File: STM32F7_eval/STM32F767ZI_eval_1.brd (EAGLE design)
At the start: 76.2 x 53.3 mm, 89 parts, among them CN1 GROVE-4P-CONN-I2C-90D, CN2 GROVE-4P-CONN-I2C-90D, CN3 GROVE-4P-CONN-I2C-90D, CN4 GROVE-4P-CONN-AN01-90D, CN5 ARDUINO_COMPAT_IF, CN6 STLINKV21_SWD_IF, CN7 WFT0750CZ09-SMD_, CN8 MCO_IF, CN9 UART_IF, Q1 PMF370XN_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

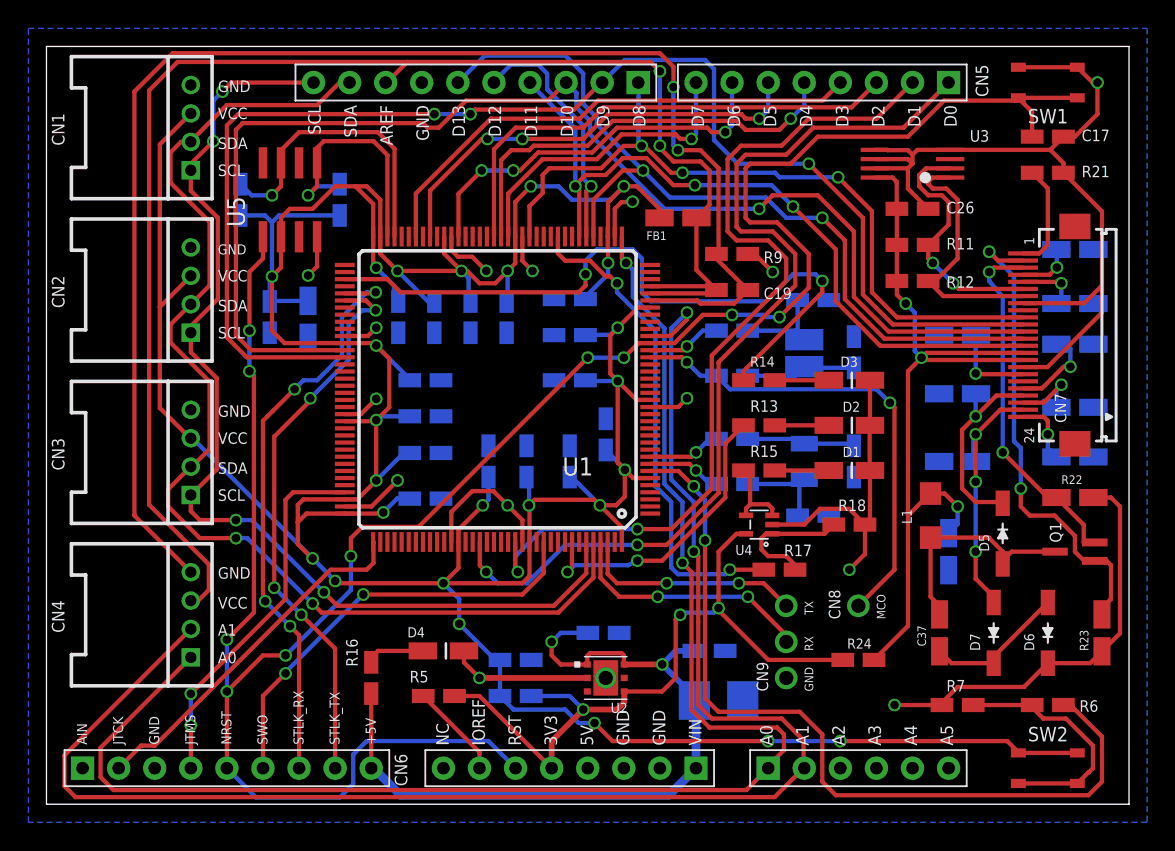
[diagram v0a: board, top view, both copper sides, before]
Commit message: 評価基板を修正
・手はんだ用パターンに修正
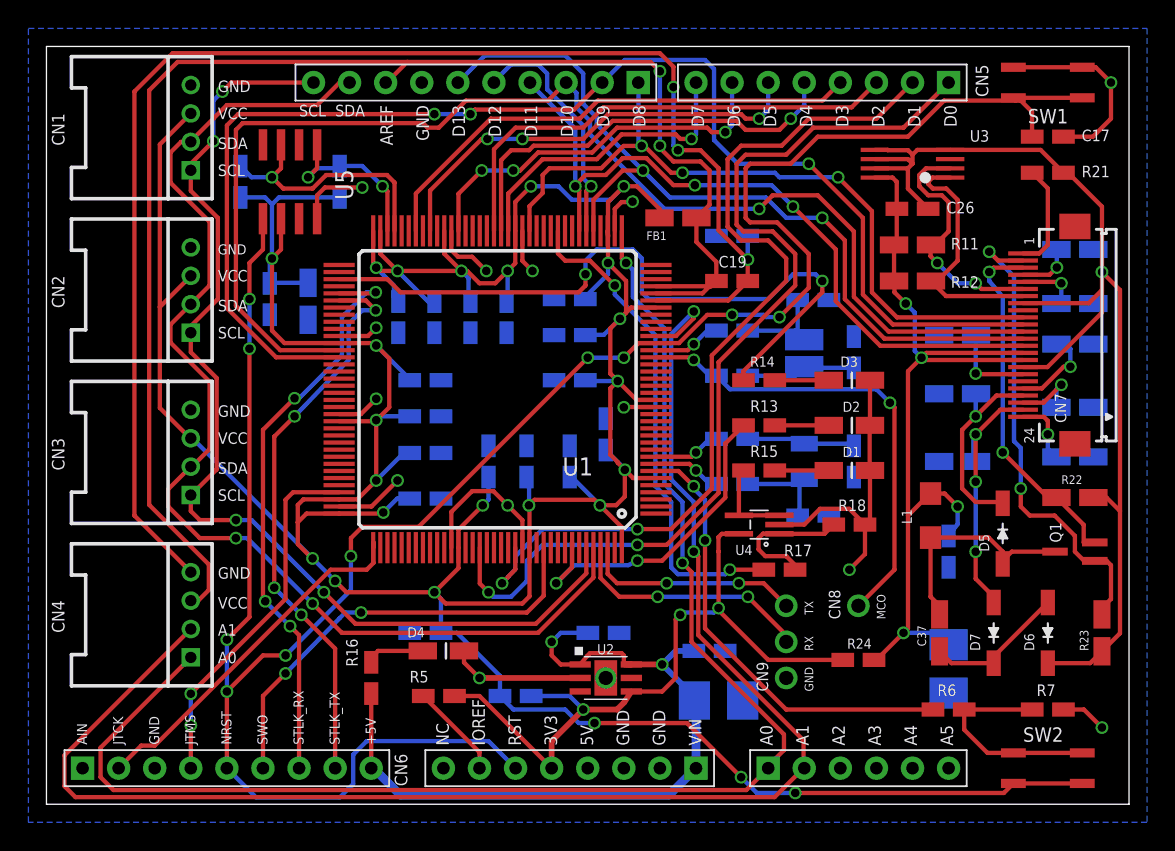
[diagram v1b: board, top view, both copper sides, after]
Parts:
- added C39: 10uF, Parts:C1210_TPST_DEV
- C38: device Parts:SMD_2012_DEV -> Parts:SMD_1608_DEV
- R11, R12: device Parts:SMD_1608_DEV -> Parts:SMD_2012_DEV
- SW1, SW2: value SKRPACE010 -> SKRPACE010_; device Parts:SKRPACE010 -> Parts:SKRPACE010_DEV
- U1: value STM32F767ZI -> STM32F767ZI_; device Parts:LQFP144 -> Parts:LQFP144_DEV
- U2: value LD39050PU33R -> LD39050PU33R_DEV; device Parts:DFN6-3X3 -> Parts:DFN6-3X3_
- U4: value TSV631AICT -> TSV631AICT_; device Parts:SC-70-5 -> Parts:SC-70-5_DEV
- moved R6 6.99 mm to (63.5, 6.67), turned to 0 degrees
- moved C22 6.63 mm to (26.7, 12.1), turned to 0 degrees
- moved R7 6.36 mm to (70.5, 6.67), turned to 180 degrees
- moved C28 1.27 mm to (15.7, 35.6)
- moved R9 1.27 mm to (48.3, 40.0), flipped to the bottom
- moved C29 1.27 mm to (18.4, 35.4)
- moved R19 1.27 mm to (13.7, 43.8)
- moved R20 1.27 mm to (20.6, 43.8)
- moved U5 1.27 mm to (17.1, 43.8)
- moved C19 0.63 mm to (48.3, 36.8)
- turned SW2 to 0 degrees
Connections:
- net 0V: now also C39.2
- net VCC_EPD: now also C39.1
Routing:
- net PC13: track 58.7 -> 31.8 mm
- net 0V: track 160.5 -> 170.2 mm
- net PB11: track 17.4 -> 12.0 mm, vias 1 -> 2
- net VCC_EPD: track 58.6 -> 62.5 mm, vias 3 -> 4
- net PB10: track 21.2 -> 18.1 mm
- net PB7: track 21.1 -> 23.7 mm
- net PC0: track 110.8 -> 108.3 mm
- net PA3: track 104.5 -> 102.1 mm
- net N$6: track 17.5 -> 15.2 mm
- net PG9: track 67.3 -> 69.2 mm
- net AVDD: track 106.1 -> 104.3 mm
- net NRST: track 158.5 -> 160.2 mm
- net PD15: track 95.6 -> 93.9 mm
- net PD14: track 91.5 -> 89.9 mm
- net PG14: track 62.8 -> 64.4 mm
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
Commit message: 評価基板を修正
・シルクの位置などを調整
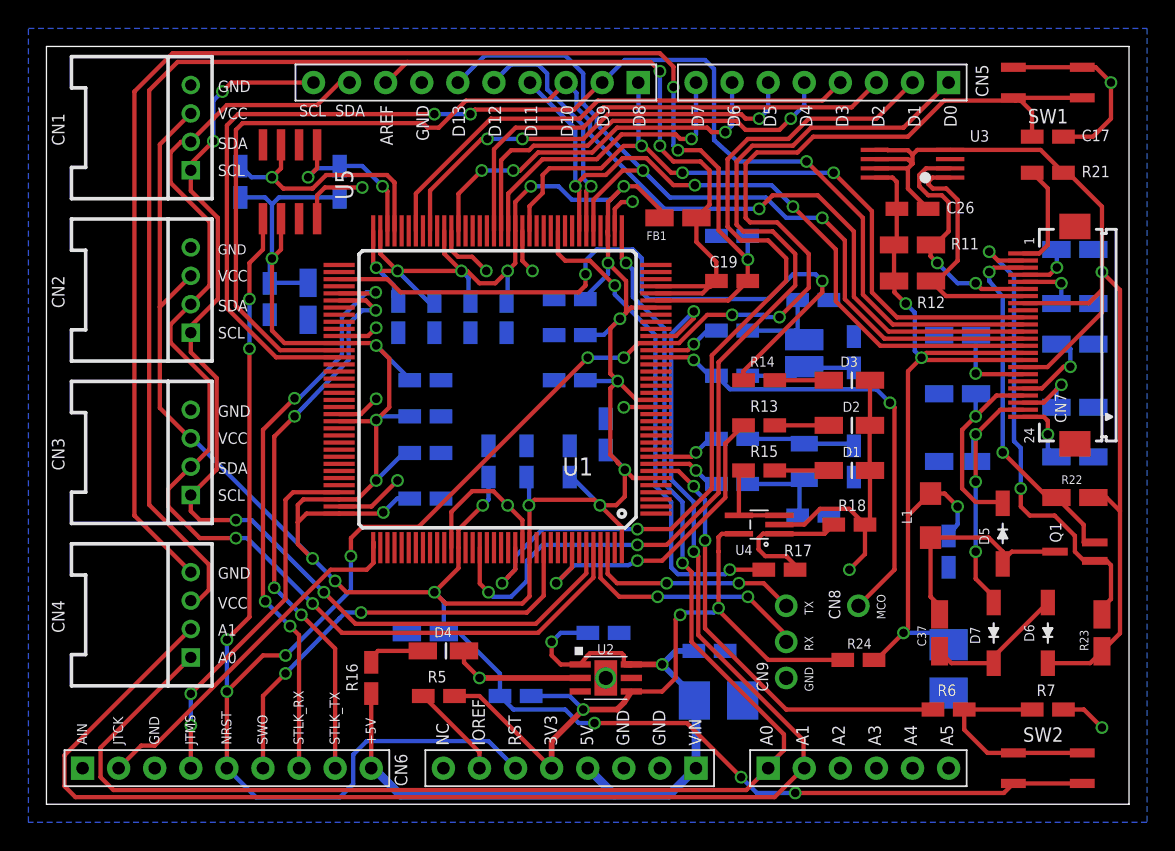
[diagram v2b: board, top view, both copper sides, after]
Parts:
- C22: device Parts:SMD_1608_DEV -> Parts:SMD_2012_DEV
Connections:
- net VIN: now also CN5.23
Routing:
- net VIN: track 55.5 -> 58.2 mm

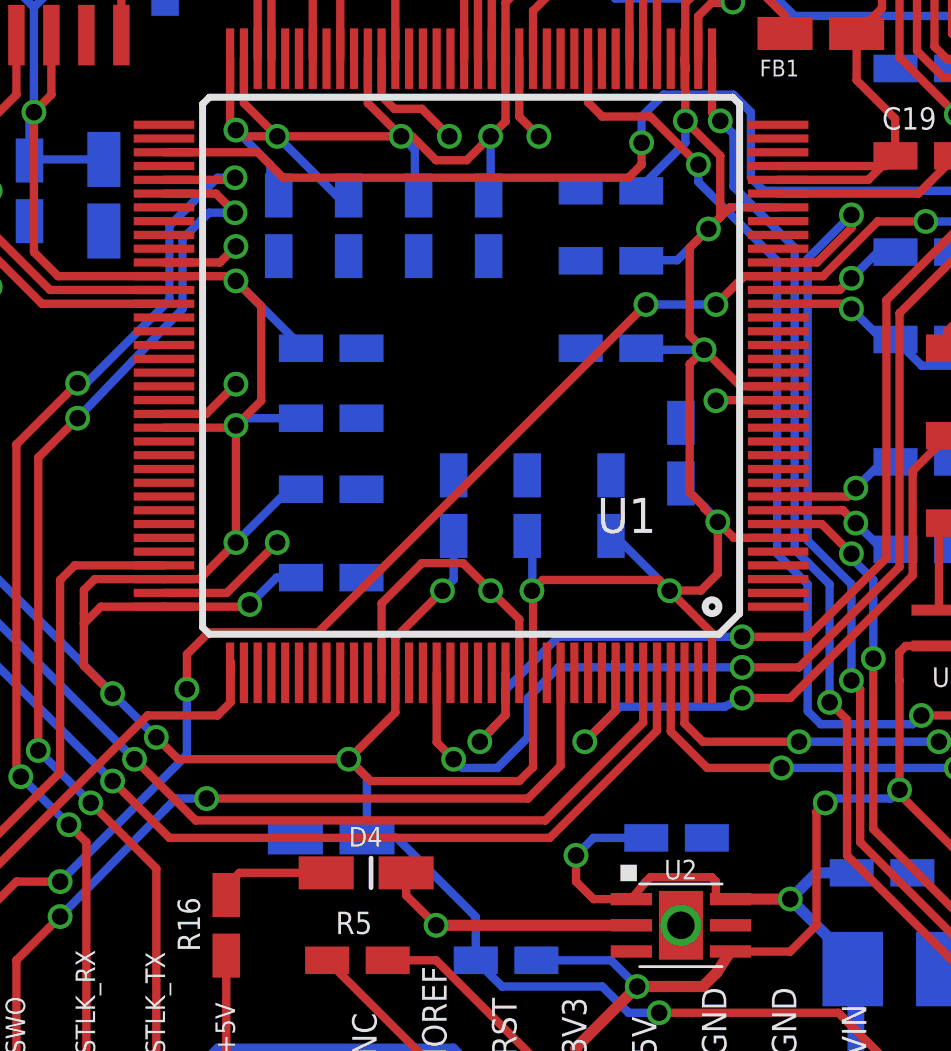
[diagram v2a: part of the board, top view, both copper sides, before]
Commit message: 評価基板を修正
・バイパスコンデンサー修正
・配線欠落箇所を修正
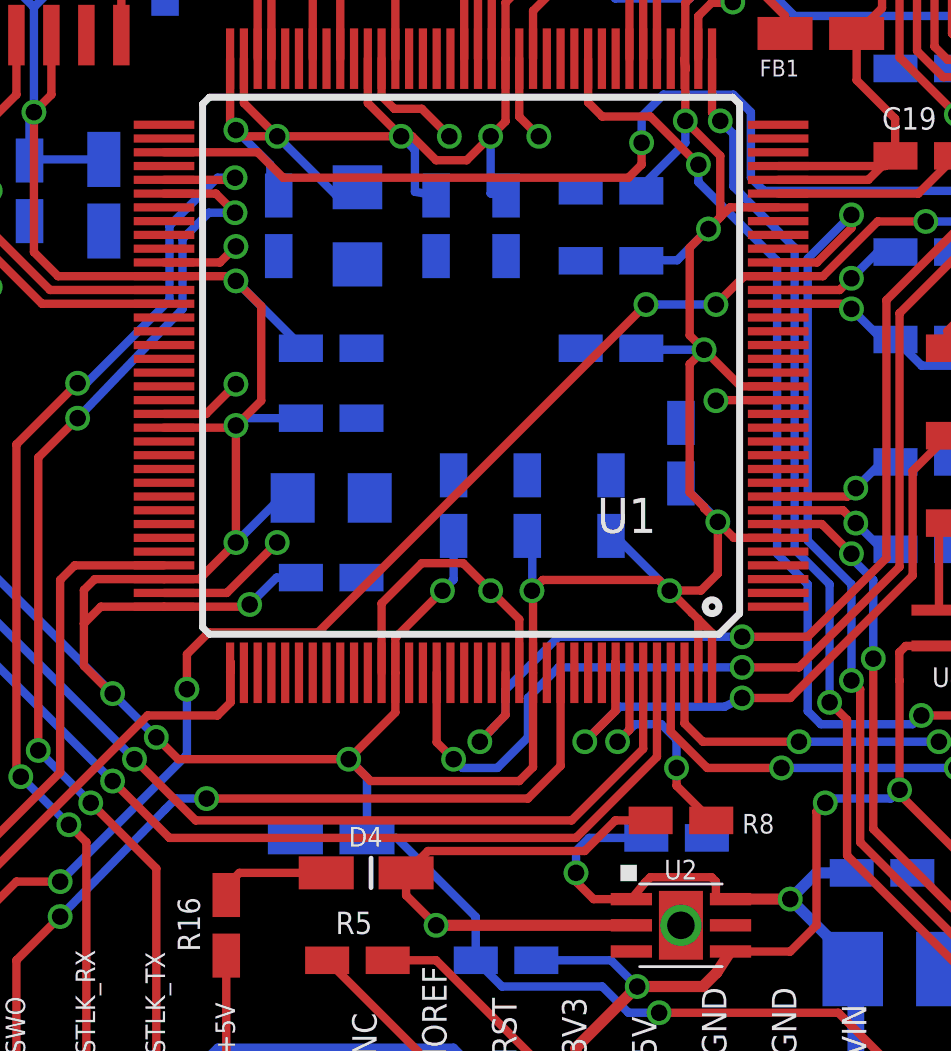
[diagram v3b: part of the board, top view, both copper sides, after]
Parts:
- added R8: 10k, Parts:SMD_1608_DEV
- C20, C21: device Parts:SMD_1608_DEV -> Parts:C1206
- moved C9 0.64 mm to (33.0, 34.3)
- moved C8 0.64 mm to (30.5, 34.3)
- moved C21 0.32 mm to (26.7, 24.4)
- moved C20 0.32 mm to (27.6, 34.3)
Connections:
- new net BOOT0: R8.1, U1.138
- net 0V: now also R8.2
- net VDD: now also U1.143
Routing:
- net 0V: track 170.2 -> 179.9 mm
- net BOOT0: track 0.00 -> 8.78 mm, vias 0 -> 2
- net VDD: track 308.2 -> 311.5 mm
- net PB9: track 81.6 -> 82.1 mm
- net PB8: track 74.6 -> 75.2 mm

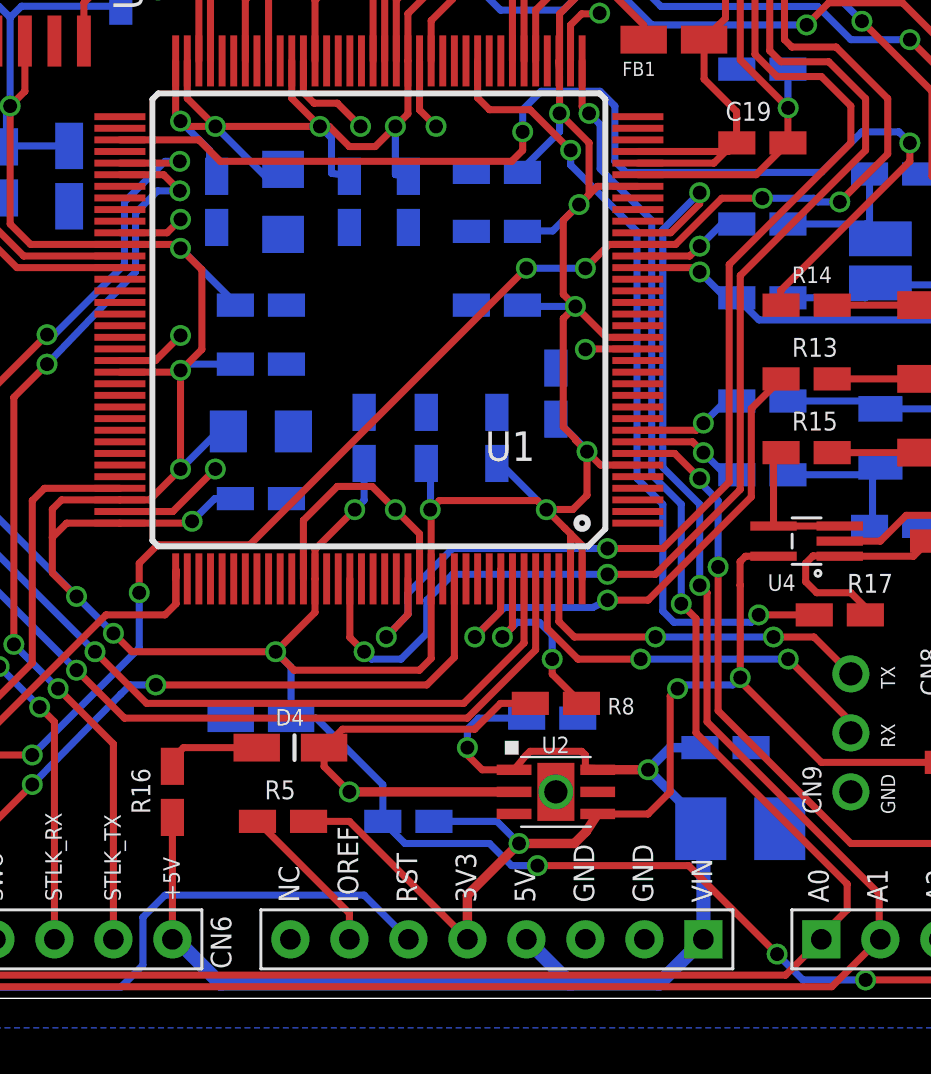
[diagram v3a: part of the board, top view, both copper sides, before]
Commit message: 評価基板を修正
・電源回路の出力側にバイパスコンデンサーを追加
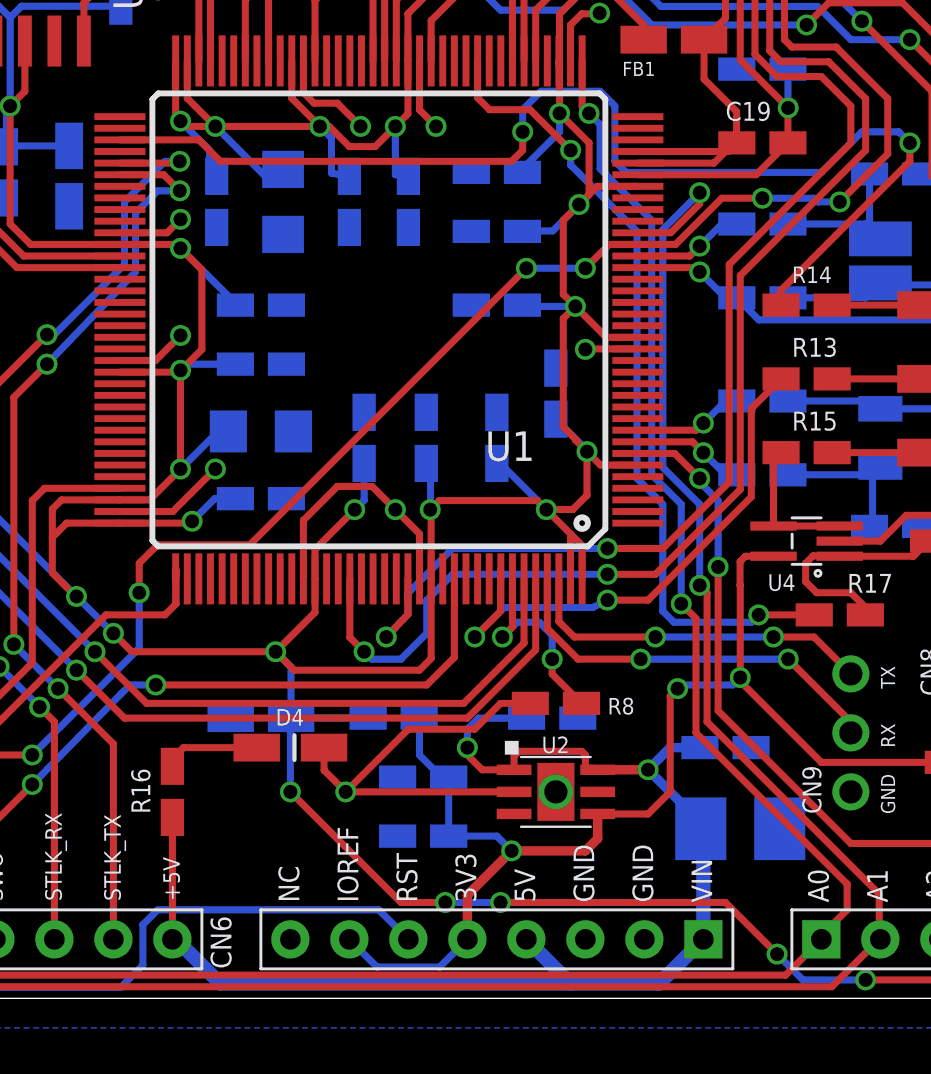
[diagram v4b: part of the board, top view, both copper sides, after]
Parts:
- removed R5: 0, Parts:SMD_1608_DEV
- added C40: 1uF X5R, Parts:SMD_1608_DEV
- added C41: 0.1uF50V, Parts:SMD_1608_DEV
- moved R10 4.49 mm to (32.4, 12.1)
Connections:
- removed net IOREF: CN5.20, R5.2
- net +3V3: now also C40.1, C41.1, CN5.20; no longer R5.1
- net 0V: now also C40.2, C41.2
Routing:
- net IOREF: track 6.72 -> 0.00 mm
- net VDD: track 311.5 -> 315.8 mm, vias 24 -> 26
- net +3V3: track 51.1 -> 53.3 mm
- net NRST: track 160.4 -> 159.7 mm

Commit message: 評価基板を修正
・定数記述を修正
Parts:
- C1, C10, C11, C12, C17, C18, C19, C2, C26, C28, C3, C38, C4, C41, C5, C6, C7, C8, C9: value 0.1uF50V -> 0.1uF
- C25, C31, C32: value 1uF35V -> 1uF
- C27, C30, C33, C34, C35, C36: value 10uF50V -> 10uF
- R6: value 330 -> 300
- R7: value 220k -> 200k
